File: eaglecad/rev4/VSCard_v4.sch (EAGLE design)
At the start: 74 parts, among them IC1 74LS244N, IC2 16C550, IC3 CY62256LL-PC, IC4 74LS244N, IC5 74LS244N, IC6 74LS00N, IC7 74LS00N, IC8 74LS244N, J1 SERIAL-TTL, J2 RCA, J3 RCA, J4 RCA, J5 RCA, Q1 10.738635mhz, Q2 2N2222, U1 TMS4416, U11 SN76489, U2 TMS9118, U3 TMS4416, U4 SN76489, Y1 1.8432mhz

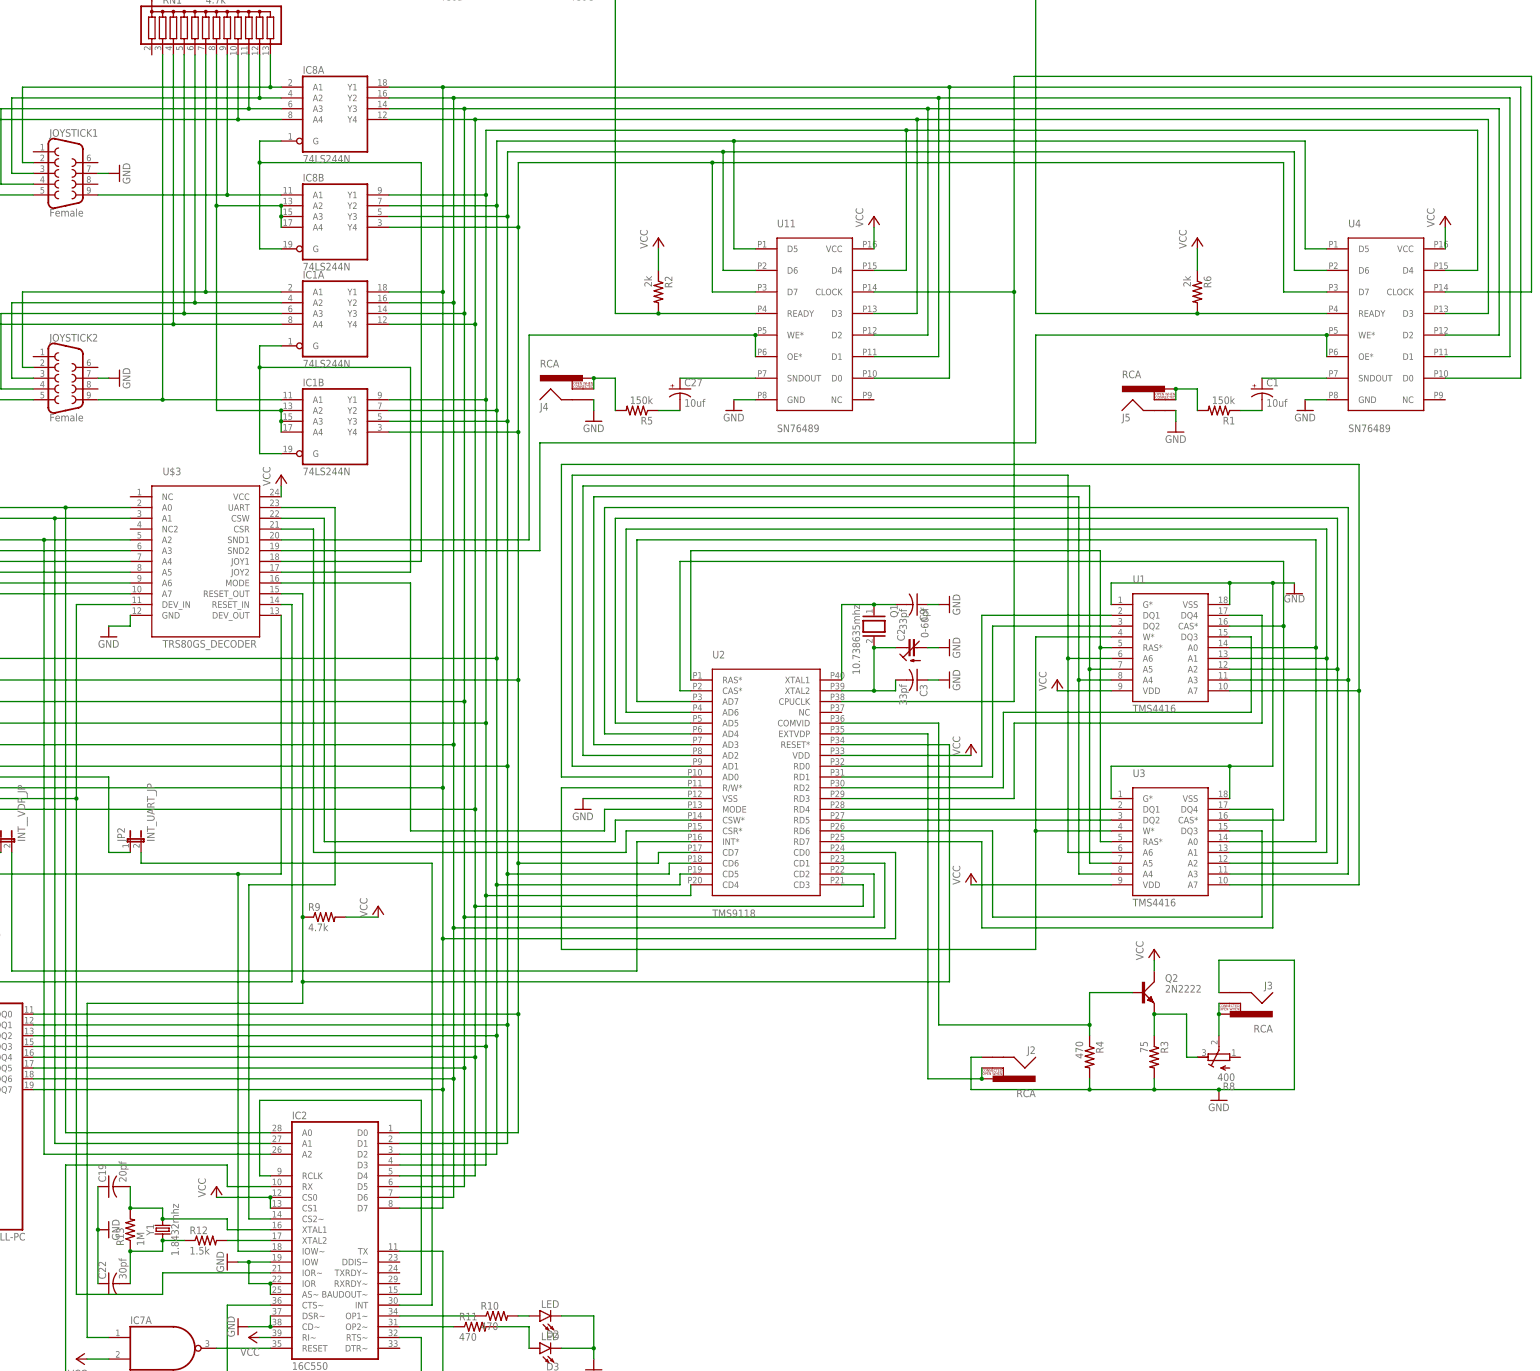
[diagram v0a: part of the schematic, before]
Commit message: got rid of extra crystal for UART -- used VDP CPUCLK output instead
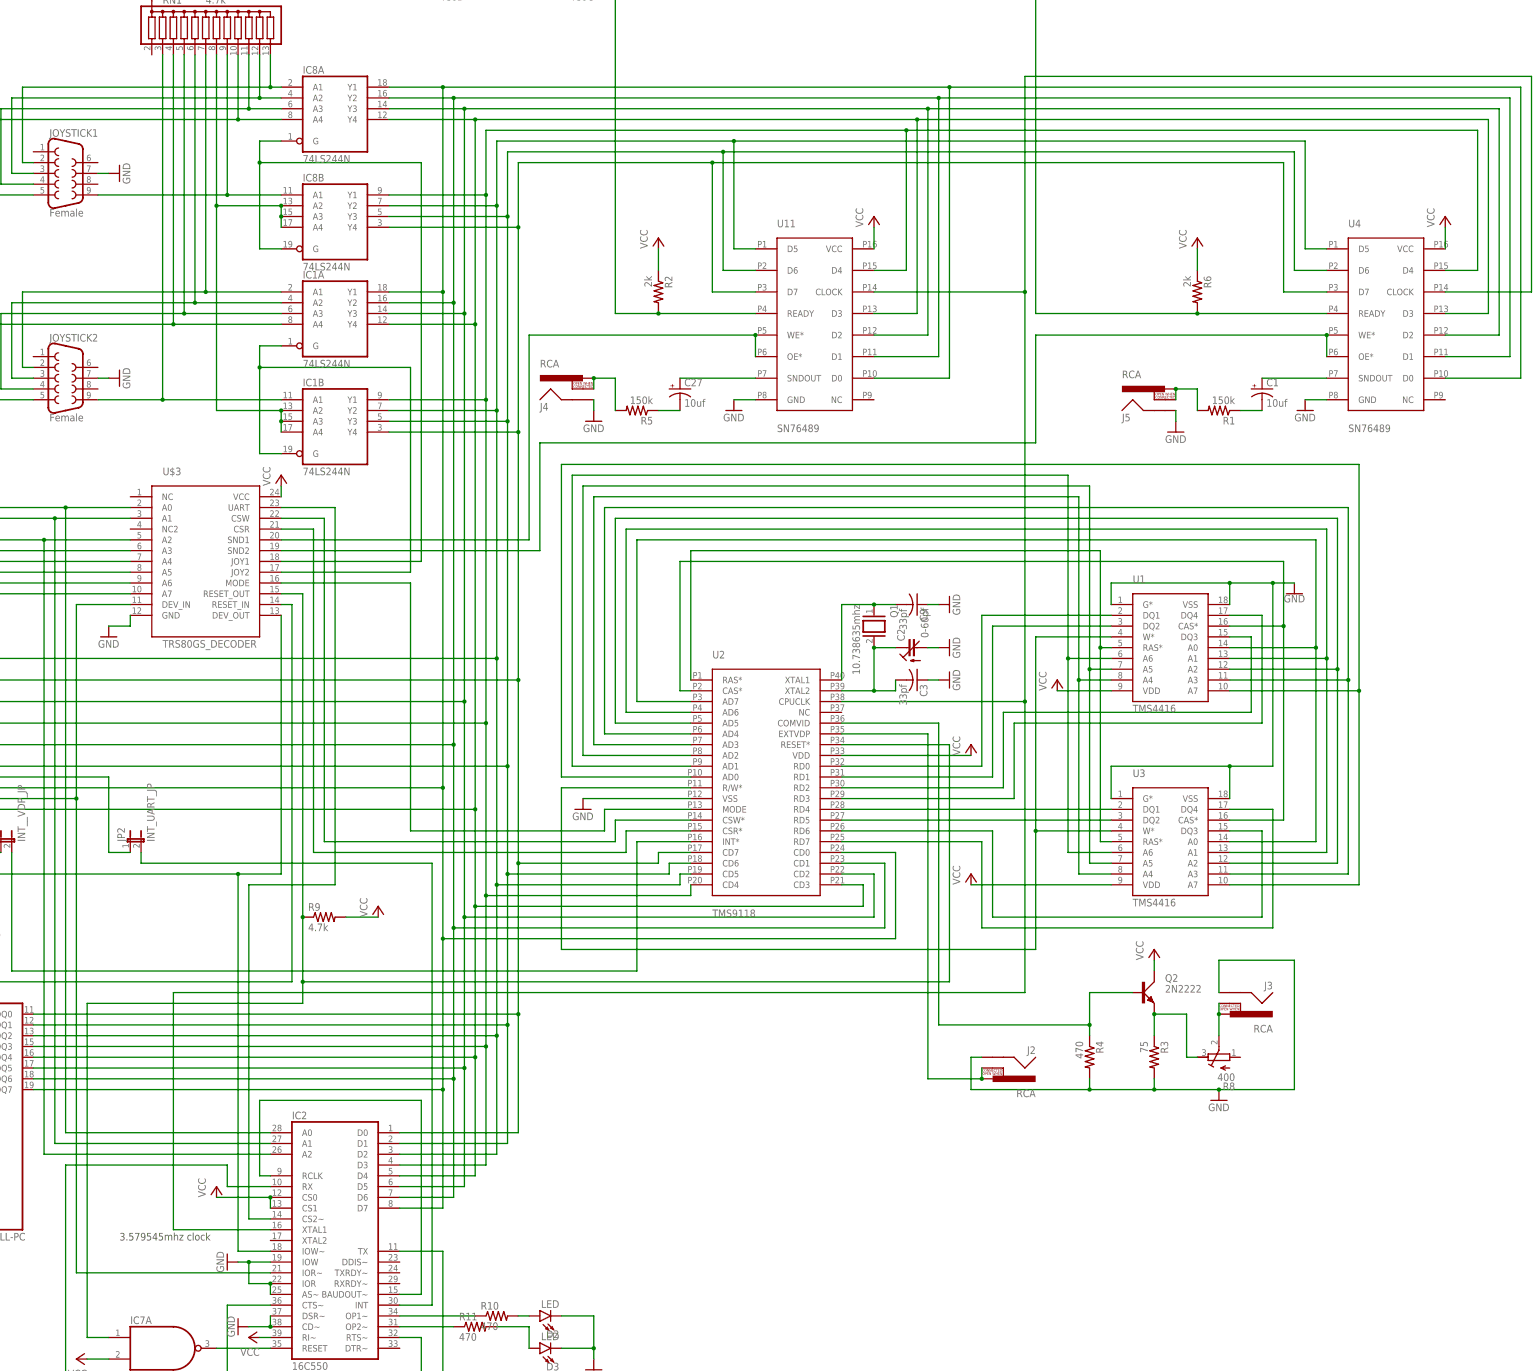
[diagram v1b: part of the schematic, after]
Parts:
- removed C19: 20pf, rcl:C-US025-025X050
- removed C22: 30pf, rcl:C-US025-025X050
- removed R12: 1.5k, resistor:R-US_0207/2V
- removed R13: 1M, resistor:R-US_0207/2V
- removed Y1: 1.8432mhz, SparkFun-Clocks:CRYSTALPTH-HC49US
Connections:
- removed net N$12: IC2G$1.XTAL2, R12.2
- removed net N$13: C22.2, R12.1, R13.1, Y1.1
- removed net N$19: C19.2, IC2G$1.XTAL1, R13.2, Y1.2
- net GND: no longer C19.1, C22.1
- net SN76489-CLOCK: now also IC2G$1.XTAL1
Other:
- note added: "3.579545mhz clock"
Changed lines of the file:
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@@
 <part name="C18" library="resistor" library_urn="urn:adsk.eagle:library:348" deviceset="C-US" device="025-025X050" package3d_urn="urn:adsk.eagle:package:26151/1" value=".1uf"/>
 <part name="P+16" library="supply1" library_urn="urn:adsk.eagle:library:371" deviceset="VCC" device=""/>
-<part name="Y1" library="SparkFun-Clocks" library_urn="urn:adsk.eagle:library:511" deviceset="CRYSTAL" device="PTH-HC49US" package3d_urn="urn:adsk.eagle:package:37515/1" value="1.8432mhz"/>
-<part name="R12" library="resistor" library_urn="urn:adsk.eagle:library:348" deviceset="R-US_" device="0207/2V" package3d_urn="urn:adsk.eagle:package:25941/1" value="1.5k"/>
-<part name="R13" library="resistor" library_urn="urn:adsk.eagle:library:348" deviceset="R-US_" device="0207/2V" package3d_urn="urn:adsk.eagle:package:25941/1" value="1M"/>
-<part name="C19" library="rcl" library_urn="urn:adsk.eagle:library:334" deviceset="C-US" device="025-025X050" package3d_urn="urn:adsk.eagle:package:23629/2" value="20pf"/>
-<part name="C22" library="rcl" library_urn="urn:adsk.eagle:library:334" deviceset="C-US" device="025-025X050" package3d_urn="urn:adsk.eagle:package:23629/2" value="30pf"/>
-<part name="GND23" library="supply1" library_urn="urn:adsk.eagle:library:371" deviceset="GND" device=""/>
 <part name="P+17" library="supply1" library_urn="urn:adsk.eagle:library:371" deviceset="VCC" device=""/>
 <part name="GND26" library="supply1" library_urn="urn:adsk.eagle:library:371" deviceset="GND" device=""/>
@@
 <sheet>
 <plain>
+<text x="81.28" y="0" size="1.778" layer="97">3.579545mhz clock</text>
 </plain>
 <instances>
@@
 <instance part="C18" gate="G$1" x="-53.34" y="210.82"/>
 <instance part="P+16" gate="VCC" x="71.12" y="-27.94" rot="R90"/>
-<instance part="Y1" gate="G$1" x="91.44" y="2.54" rot="R90"/>
-<instance part="R12" gate="G$1" x="101.6" y="0"/>
-<instance part="R13" gate="G$1" x="83.82" y="2.54" rot="R90"/>
-<instance part="C19" gate="G$1" x="78.74" y="12.7" rot="R90"/>
-<instance part="C22" gate="G$1" x="78.74" y="-10.16" rot="R90"/>
-<instance part="GND23" gate="1" x="78.74" y="2.54" rot="R90"/>
 <instance part="P+17" gate="VCC" x="111.76" y="-22.86" rot="R90"/>
 <instance part="GND26" gate="1" x="109.22" y="-20.32" rot="R270"/>
@@
 </segment>
 <segment>
-<pinref part="C19" gate="G$1" pin="1"/>
-<pinref part="GND23" gate="1" pin="GND"/>
-<wire x1="76.2" y1="12.7" x2="76.2" y2="2.54" width="0.1524" layer="91"/>
-<pinref part="C22" gate="G$1" pin="1"/>
-<wire x1="76.2" y1="-10.16" x2="76.2" y2="2.54" width="0.1524" layer="91"/>
-<junction x="76.2" y="2.54"/>
-</segment>
-<segment>
 <pinref part="IC2" gate="G$1" pin="CD~"/>
 <pinref part="GND26" gate="1" pin="GND"/>
@@
 <wire x1="414.02" y1="223.52" x2="414.02" y2="274.32" width="0.1524" layer="91"/>
 <pinref part="U11" gate="G$1" pin="CLOCK"/>
-<wire x1="259.08" y1="223.52" x2="292.1" y2="223.52" width="0.1524" layer="91"/>
-<wire x1="414.02" y1="274.32" x2="292.1" y2="274.32" width="0.1524" layer="91"/>
-<wire x1="292.1" y1="274.32" x2="292.1" y2="223.52" width="0.1524" layer="91"/>
+<wire x1="259.08" y1="223.52" x2="294.64" y2="223.52" width="0.1524" layer="91"/>
+<wire x1="414.02" y1="274.32" x2="294.64" y2="274.32" width="0.1524" layer="91"/>
+<wire x1="294.64" y1="274.32" x2="294.64" y2="223.52" width="0.1524" layer="91"/>
 <pinref part="U2" gate="G$1" pin="CPUCLK"/>
-<wire x1="251.46" y1="127" x2="292.1" y2="127" width="0.1524" layer="91"/>
-<wire x1="292.1" y1="127" x2="292.1" y2="223.52" width="0.1524" layer="91"/>
-<junction x="292.1" y="223.52"/>
+<wire x1="251.46" y1="127" x2="294.64" y2="127" width="0.1524" layer="91"/>
+<wire x1="294.64" y1="127" x2="294.64" y2="223.52" width="0.1524" layer="91"/>
+<junction x="294.64" y="223.52"/>
+<wire x1="294.64" y1="127" x2="294.64" y2="58.42" width="0.1524" layer="91"/>
+<junction x="294.64" y="127"/>
+<wire x1="294.64" y1="58.42" x2="93.98" y2="58.42" width="0.1524" layer="91"/>
+<wire x1="93.98" y1="58.42" x2="93.98" y2="2.54" width="0.1524" layer="91"/>
+<pinref part="IC2" gate="G$1" pin="XTAL1"/>
+<wire x1="93.98" y1="2.54" x2="116.84" y2="2.54" width="0.1524" layer="91"/>
 </segment>
 </net>
@@
 <wire x1="71.12" y1="149.86" x2="83.82" y2="149.86" width="0.1524" layer="91"/>
 <pinref part="U$3" gate="G$1" pin="DEV_IN"/>
-<wire x1="71.12" y1="104.14" x2="71.12" y2="-12.7" width="0.1524" layer="91"/>
+<wire x1="71.12" y1="104.14" x2="71.12" y2="-7.62" width="0.1524" layer="91"/>
 <junction x="71.12" y="104.14"/>
 <pinref part="IC2" gate="G$1" pin="IOR~"/>
-<wire x1="116.84" y1="-7.62" x2="91.44" y2="-7.62" width="0.1524" layer="91"/>
-<wire x1="91.44" y1="-7.62" x2="91.44" y2="-12.7" width="0.1524" layer="91"/>
-<wire x1="91.44" y1="-12.7" x2="71.12" y2="-12.7" width="0.1524" layer="91"/>
+<wire x1="116.84" y1="-7.62" x2="71.12" y2="-7.62" width="0.1524" layer="91"/>
 </segment>
 </net>
@@
 </segment>
 </net>
-<net name="N$12" class="0">
-<segment>
-<pinref part="IC2" gate="G$1" pin="XTAL2"/>
-<pinref part="R12" gate="G$1" pin="2"/>
-<wire x1="116.84" y1="0" x2="106.68" y2="0" width="0.1524" layer="91"/>
-</segment>
-</net>
-<net name="N$13" class="0">
-<segment>
-<pinref part="R12" gate="G$1" pin="1"/>
-<pinref part="Y1" gate="G$1" pin="1"/>
-<wire x1="96.52" y1="0" x2="91.44" y2="0" width="0.1524" layer="91"/>
-<pinref part="R13" gate="G$1" pin="1"/>
-<wire x1="83.82" y1="-2.54" x2="91.44" y2="-2.54" width="0.1524" layer="91"/>
-<wire x1="91.44" y1="-2.54" x2="91.44" y2="0" width="0.1524" layer="91"/>
-<junction x="91.44" y="0"/>
-<pinref part="C22" gate="G$1" pin="2"/>
-<wire x1="83.82" y1="-2.54" x2="83.82" y2="-10.16" width="0.1524" layer="91"/>
-<junction x="83.82" y="-2.54"/>
-</segment>
-</net>
-<net name="N$19" class="0">
-<segment>
-<pinref part="IC2" gate="G$1" pin="XTAL1"/>
-<wire x1="116.84" y1="2.54" x2="106.68" y2="2.54" width="0.1524" layer="91"/>
-<wire x1="106.68" y1="2.54" x2="106.68" y2="5.08" width="0.1524" layer="91"/>
-<pinref part="Y1" gate="G$1" pin="2"/>
-<wire x1="106.68" y1="5.08" x2="91.44" y2="5.08" width="0.1524" layer="91"/>
-<wire x1="91.44" y1="5.08" x2="91.44" y2="7.62" width="0.1524" layer="91"/>
-<junction x="91.44" y="5.08"/>
-<pinref part="R13" gate="G$1" pin="2"/>
-<wire x1="91.44" y1="7.62" x2="83.82" y2="7.62" width="0.1524" layer="91"/>
-<pinref part="C19" gate="G$1" pin="2"/>
-<wire x1="83.82" y1="12.7" x2="83.82" y2="7.62" width="0.1524" layer="91"/>
-<junction x="83.82" y="7.62"/>
-</segment>
-</net>
 <net name="N$23" class="0">
 <segment>
@@
 </sheet>
 </sheets>
+<errors>
+</errors>
 </schematic>
 </drawing>
